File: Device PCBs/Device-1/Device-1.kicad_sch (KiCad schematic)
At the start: 29 parts, among them U2 MAX487E

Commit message: Device 1 PCB is finished
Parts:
- C1: renamed from C?; footprint (none) -> Capacitor_SMD:CP_Elec_6.3x5.7
- C2: renamed from C?; footprint (none) -> Capacitor_SMD:C_1206_3216Metric
- D1, D2, D3, D4, D5, D6, D7, D8, D9: renamed from D?; footprint (none) -> LED_SMD:LED_1206_3216Metric
- R1, R10, R11, R12, R13, R14, R15, R2, R3, R4, R5, R6, R7, R8, R9: renamed from R?; footprint (none) -> Resistor_SMD:R_1206_3216Metric
- U1: renamed from U?; footprint (none) -> Device_1_project_footprints:EBYTE-E32-433T20D
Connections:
- net EBYTE_AUX: now also A1.5 (D2); no longer A1.9 (D6)
- net EBYTE_RX: now also A1.7 (D4), D6.2 (A); no longer A1.8 (D5), D4.2 (A)
- net EBYTE_TX: now also A1.6 (D3), D4.2 (A); no longer A1.7 (D4), D6.2 (A)
- net M0: now also A1.9 (D6); no longer A1.5 (D2)
- net M1: now also A1.8 (D5); no longer A1.6 (D3)
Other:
- moved on the sheet: A1

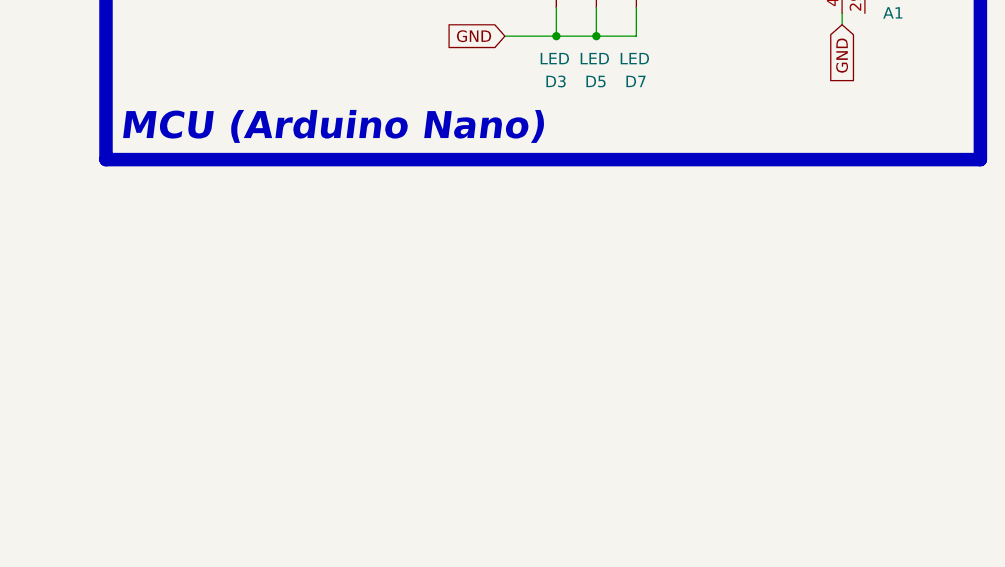
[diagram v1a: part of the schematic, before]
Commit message: slave config.h  and tescom_SDDPV2200M
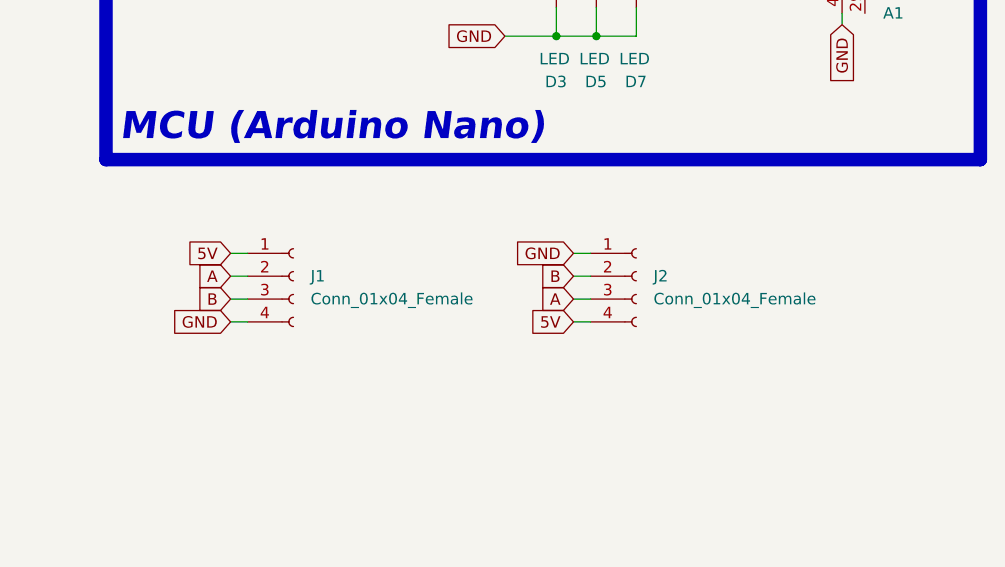
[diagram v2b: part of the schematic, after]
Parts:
- added J1: Conn_01x04_Female, Connector_PinSocket_2.54mm:PinSocket_1x04_P2.54mm_Vertical, symbol Connector:Conn_01x04_Female
- added J2: Conn_01x04_Female, Device_1_project_footprints:output_vias, symbol Connector:Conn_01x04_Female
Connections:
- net 5V: now also J1.1 (Pin_1), J2.4 (Pin_4)
- net A: now also J1.2 (Pin_2), J2.3 (Pin_3)
- net B: now also J1.3 (Pin_3), J2.2 (Pin_2)
- net GND: now also J1.4 (Pin_4), J2.1 (Pin_1)
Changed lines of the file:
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@@
+    (stroke (width 0) (type default) (color 0 0 0 0))
+  )
+  (wire (pts (xy 200.025 111.76) (xy 201.93 111.76))
     (stroke (width 0) (type default) (color 0 0 0 0))
   )
@@
     (stroke (width 0) (type default) (color 0 0 0 0))
   )
+  (wire (pts (xy 238.125 111.76) (xy 240.03 111.76))
+    (stroke (width 0) (type default) (color 0 0 0 0))
+  )
   (wire (pts (xy 59.182 91.821) (xy 76.327 91.821))
     (stroke (width 0) (type default) (color 0 0 0 0))
@@
     (stroke (width 0) (type default) (color 0 0 0 0))
   )
+  (wire (pts (xy 238.125 109.22) (xy 240.03 109.22))
+    (stroke (width 0) (type default) (color 0 0 0 0))
+  )
   (wire (pts (xy 248.92 54.61) (xy 255.27 54.61))
     (stroke (width 0) (type default) (color 0 0 0 0))
   )
+  (wire (pts (xy 238.125 114.3) (xy 240.03 114.3))
+    (stroke (width 0) (type default) (color 0 0 0 0))
+  )
   (wire (pts (xy 244.475 41.275) (xy 244.475 52.07))
     (stroke (width 0) (type default) (color 0 0 0 0))
@@
     (stroke (width 0) (type default) (color 0 0 0 0))
   )
+  (wire (pts (xy 238.125 116.84) (xy 240.03 116.84))
+    (stroke (width 0) (type default) (color 0 0 0 0))
+  )
   (wire (pts (xy 235.585 22.86) (xy 235.585 24.765))
     (stroke (width 0) (type default) (color 0 0 0 0))
@@
     (stroke (width 0) (type default) (color 0 0 0 0))
   )
+  (wire (pts (xy 200.025 109.22) (xy 201.93 109.22))
+    (stroke (width 0) (type default) (color 0 0 0 0))
+  )
   (wire (pts (xy 151.384 147.574) (xy 148.209 147.574))
     (stroke (width 0) (type default) (color 0 0 0 0))
@@
     (stroke (width 0.67) (type default) (color 0 0 0 0))
   )
+  (wire (pts (xy 200.025 114.3) (xy 201.93 114.3))
+    (stroke (width 0) (type default) (color 0 0 0 0))
+  )
   (wire (pts (xy 236.22 81.915) (xy 236.22 85.09))
+    (stroke (width 0) (type default) (color 0 0 0 0))
+  )
+  (wire (pts (xy 200.025 116.84) (xy 201.93 116.84))
     (stroke (width 0) (type default) (color 0 0 0 0))
   )
@@
     )
   )
+  (global_label "B" (shape input) (at 238.125 111.76 180) (fields_autoplaced)
+    (effects (font (size 1.27 1.27)) (justify right))
+    (property "Intersheet References" "${INTERSHEET_REFS}" (id 0) (at 234.4419 111.8394 0)
+      (effects (font (size 1.27 1.27)) (justify right) hide)
+    )
+  )
   (global_label "B" (shape input) (at 106.807 70.866 0) (fields_autoplaced)
     (effects (font (size 1.27 1.27)) (justify left))
@@
     )
   )
+  (global_label "GND" (shape input) (at 238.125 109.22 180) (fields_autoplaced)
+    (effects (font (size 1.27 1.27)) (justify right))
+    (property "Intersheet References" "${INTERSHEET_REFS}" (id 0) (at 231.8414 109.1406 0)
+      (effects (font (size 1.27 1.27)) (justify right) hide)
+    )
+  )
   (global_label "5V" (shape input) (at 151.384 165.354 0) (fields_autoplaced)
     (effects (font (size 1.27 1.27)) (justify left))
@@
     )
   )
+  (global_label "5V" (shape input) (at 200.025 109.22 180) (fields_autoplaced)
+    (effects (font (size 1.27 1.27)) (justify right))
+    (property "Intersheet References" "${INTERSHEET_REFS}" (id 0) (at 195.3138 109.2994 0)
+      (effects (font (size 1.27 1.27)) (justify right) hide)
+    )
+  )
   (global_label "RS485_SS_TX_PIN" (shape input) (at 50.927 78.486 180) (fields_autoplaced)
     (effects (font (size 1.27 1.27)) (justify right))
@@
     )
   )
+  (global_label "A" (shape input) (at 238.125 114.3 180) (fields_autoplaced)
+    (effects (font (size 1.27 1.27)) (justify right))
+    (property "Intersheet References" "${INTERSHEET_REFS}" (id 0) (at 234.6233 114.3794 0)
+      (effects (font (size 1.27 1.27)) (justify right) hide)
+    )
+  )
+  (global_label "GND" (shape input) (at 200.025 116.84 180) (fields_autoplaced)
+    (effects (font (size 1.27 1.27)) (justify right))
+    (property "Intersheet References" "${INTERSHEET_REFS}" (id 0) (at 193.7414 116.7606 0)
+      (effects (font (size 1.27 1.27)) (justify right) hide)
+    )
+  )
   (global_label "GND" (shape input) (at 228.6 22.86 180) (fields_autoplaced)
     (effects (font (size 1.27 1.27)) (justify right))
@@
     )
   )
+  (global_label "A" (shape input) (at 200.025 111.76 180) (fields_autoplaced)
+    (effects (font (size 1.27 1.27)) (justify right))
+    (property "Intersheet References" "${INTERSHEET_REFS}" (id 0) (at 196.5233 111.8394 0)
+      (effects (font (size 1.27 1.27)) (justify right) hide)
+    )
+  )
+  (global_label "B" (shape input) (at 200.025 114.3 180) (fields_autoplaced)
+    (effects (font (size 1.27 1.27)) (justify right))
+    (property "Intersheet References" "${INTERSHEET_REFS}" (id 0) (at 196.3419 114.3794 0)
+      (effects (font (size 1.27 1.27)) (justify right) hide)
+    )
+  )
   (global_label "EBYTE_RX" (shape input) (at 59.944 170.942 0) (fields_autoplaced)
     (effects (font (size 1.27 1.27)) (justify left))
@@
     (effects (font (size 1.27 1.27)) (justify right))
     (property "Intersheet References" "${INTERSHEET_REFS}" (id 0) (at 88.9476 93.3572 90)
+      (effects (font (size 1.27 1.27)) (justify right) hide)
+    )
+  )
+  (global_label "5V" (shape input) (at 238.125 116.84 180) (fields_autoplaced)
+    (effects (font (size 1.27 1.27)) (justify right))
+    (property "Intersheet References" "${INTERSHEET_REFS}" (id 0) (at 233.4138 116.9194 0)
       (effects (font (size 1.27 1.27)) (justify right) hide)
     )
@@
     (pin "2")
   )
+  (symbol (lib_id "Connector:Conn_01x04_Female") (at 207.01 111.76 0) (unit 1)
+    (in_bom yes) (on_board yes) (fields_autoplaced)
+    (property "Reference" "J1" (id 0) (at 208.915 111.7599 0)
+      (effects (font (size 1.27 1.27)) (justify left))
+    )
+    (property "Value" "Conn_01x04_Female" (id 1) (at 208.915 114.2999 0)
+      (effects (font (size 1.27 1.27)) (justify left))
+    )
+    (property "Footprint" "Connector_PinSocket_2.54mm:PinSocket_1x04_P2.54mm_Vertical" (id 2) (at 207.01 111.76 0)
+      (effects (font (size 1.27 1.27)) hide)
+    )
+    (property "Datasheet" "~" (id 3) (at 207.01 111.76 0)
+      (effects (font (size 1.27 1.27)) hide)
+    )
+    (pin "1")
+    (pin "2")
+    (pin "3")
+    (pin "4")
+  )
   (symbol (lib_id "Device:R") (at 244.475 28.575 180) (unit 1)
     (in_bom yes) (on_board yes)
@@
     (pin "1")
     (pin "2")
+  )
+  (symbol (lib_id "Connector:Conn_01x04_Female") (at 245.11 111.76 0) (unit 1)
+    (in_bom yes) (on_board yes) (fields_autoplaced)
+    (property "Reference" "J2" (id 0) (at 247.015 111.7599 0)
+      (effects (font (size 1.27 1.27)) (justify left))
+    )
+    (property "Value" "Conn_01x04_Female" (id 1) (at 247.015 114.2999 0)
+      (effects (font (size 1.27 1.27)) (justify left))
+    )
+    (property "Footprint" "Device_1_project_footprints:output_vias" (id 2) (at 245.11 111.76 0)
+      (effects (font (size 1.27 1.27)) hide)
+    )
+    (property "Datasheet" "~" (id 3) (at 245.11 111.76 0)
+      (effects (font (size 1.27 1.27)) hide)
+    )
+    (pin "1")
+    (pin "2")
+    (pin "3")
+    (pin "4")
   )
   (symbol (lib_id "Device:LED") (at 248.92 37.465 270) (unit 1)
@@
       (reference "D9") (unit 1) (value "LED") (footprint "LED_SMD:LED_1206_3216Metric")
     )
+    (path "/2e2cdef3-d221-46c3-96bb-35bd60ef0027"
+      (reference "J1") (unit 1) (value "Conn_01x04_Female") (footprint "Connector_PinSocket_2.54mm:PinSocket_1x04_P2.54mm_Vertical")
+    )
+    (path "/4897caee-f680-4d16-969b-7506d8f8b91f"
+      (reference "J2") (unit 1) (value "Conn_01x04_Female") (footprint "Device_1_project_footprints:output_vias")
+    )
     (path "/ababefe4-93dd-4ef0-80c7-1b4dc99fb798"

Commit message: Device 1 PCB is finished
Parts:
- added U10, U11, U12, U13, U14, U15, U16, U17, U18, U19, U20, U21, U22, U23, U3, U4, U5, U6, U7, U8, U9: signle_via, Device_1_project_footprints:single_via, symbol device_1_project_symbols:signle_via
- C1: footprint Capacitor_SMD:CP_Elec_6.3x5.7 -> Capacitor_SMD:CP_Elec_6.3x5.2
- D1, D2, D3, D8, D9: footprint LED_SMD:LED_1206_3216Metric -> Device_1_project_footprints:lm281B-3000K
- D4, D5, D6, D7: footprint LED_SMD:LED_1206_3216Metric -> Device_1_project_footprints:lm281B-6500K
- renumbered A1 to ArduinoNano
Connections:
- net 5V: now also J1.4 (Pin_4), U20.1 (Via); no longer J1.1 (Pin_1)
- net A: now also J2.2 (Pin_2); no longer J2.3 (Pin_3)
- net B: now also J1.1 (Pin_1), J2.1 (Pin_1); no longer J1.3 (Pin_3), J2.2 (Pin_2)
- net GND: now also J1.3 (Pin_3), J2.3 (Pin_3); no longer J1.4 (Pin_4), J2.1 (Pin_1)
- net at ArduinoNano.1 (D1/TX): now also U22.1 (Via)
- net at ArduinoNano.13 (D10): now also U3.1 (Via)
- net at ArduinoNano.14 (D11): now also U4.1 (Via)
- net at ArduinoNano.15 (D12): now also U5.1 (Via)
- net at ArduinoNano.16 (D13): now also U6.1 (Via)
- net at ArduinoNano.17 (3V3): now also U21.1 (Via)
- net at ArduinoNano.18 (AREF): now also U10.1 (Via)
- net at ArduinoNano.19 (A0): now also U11.1 (Via)
- net at ArduinoNano.2 (D0/RX): now also U23.1 (Via)
- net at ArduinoNano.20 (A1): now also U12.1 (Via)
- net at ArduinoNano.21 (A2): now also U13.1 (Via)
- net at ArduinoNano.22 (A3): now also U14.1 (Via)
- net at ArduinoNano.23 (A4): now also U15.1 (Via)
- net at ArduinoNano.24 (A5): now also U16.1 (Via)
- net at ArduinoNano.25 (A6): now also U17.1 (Via)
- net at ArduinoNano.26 (A7): now also U18.1 (Via)
- net at ArduinoNano.28 (~{RESET}): now also U8.1 (Via)
- net at ArduinoNano.29 (GND): now also U7.1 (Via)
- net at ArduinoNano.3 (~{RESET}): now also U9.1 (Via)
- net at ArduinoNano.30 (VIN): now also U19.1 (Via)
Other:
- moved on the sheet: ArduinoNano, D2, D3, D4, D5, D6, D7, D8, D9, R10, R11, R12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

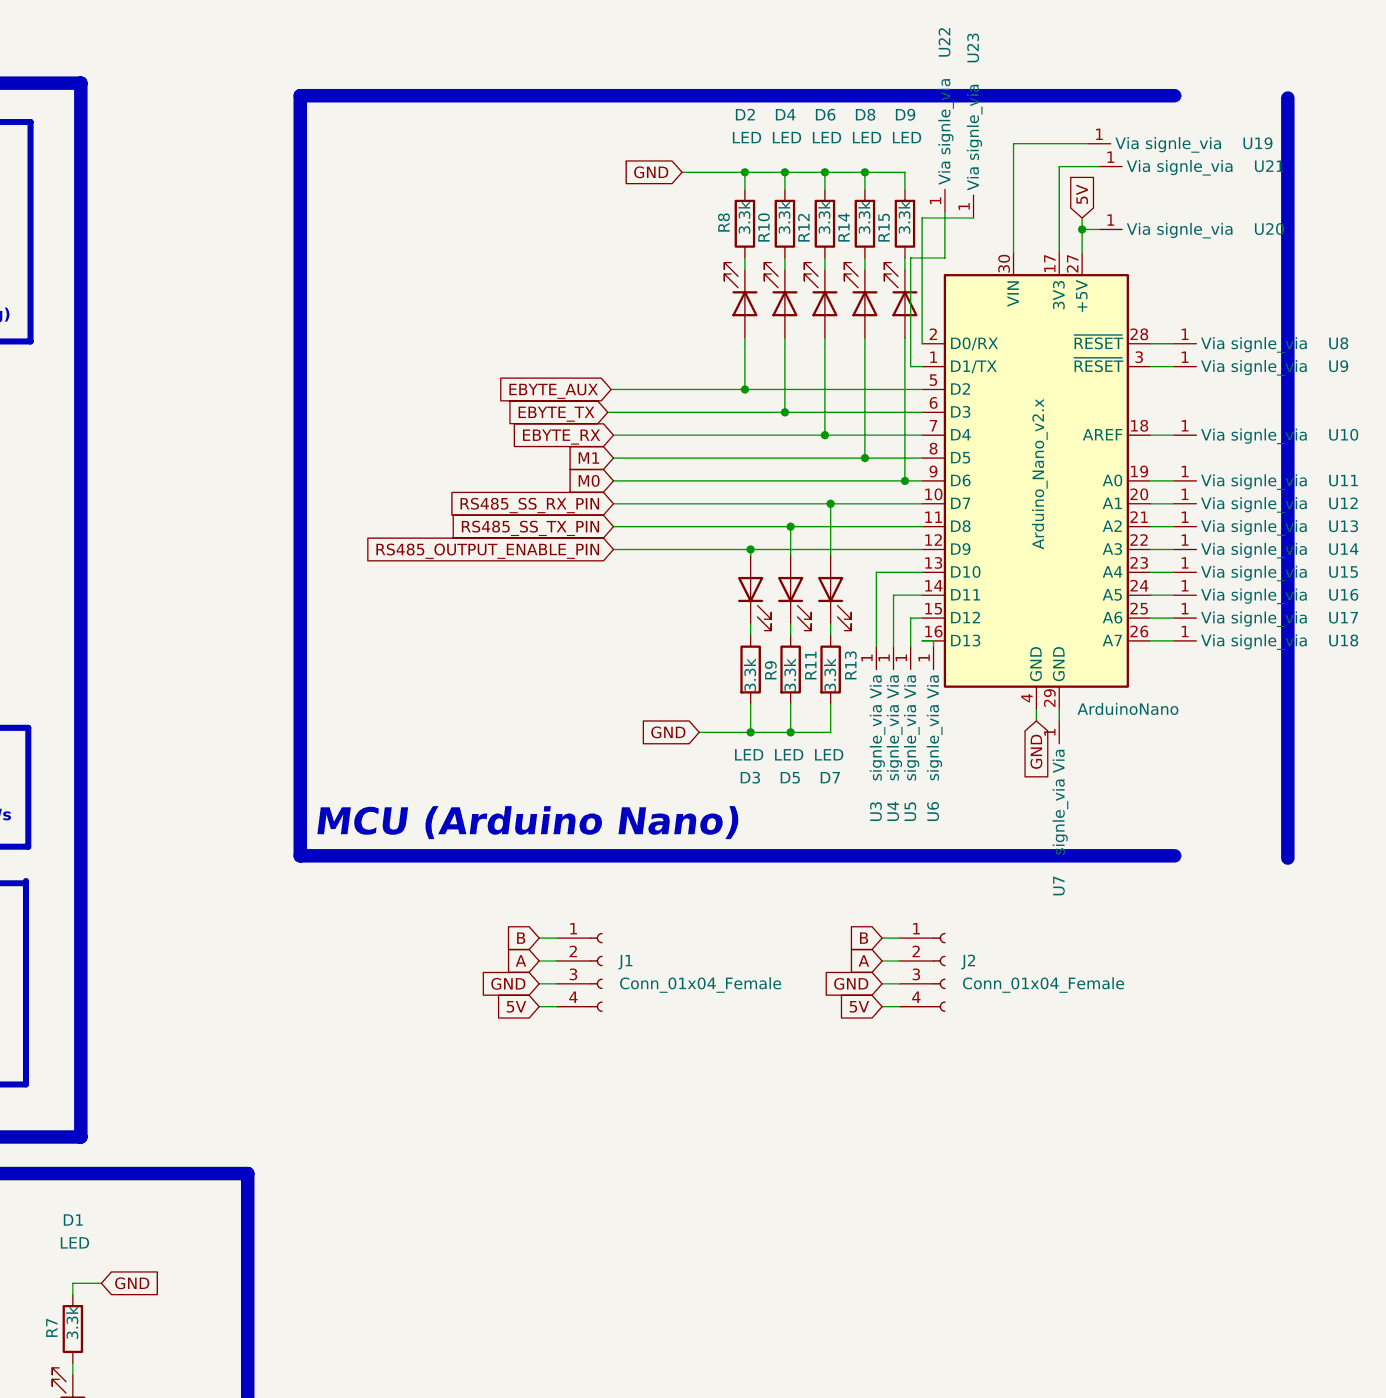
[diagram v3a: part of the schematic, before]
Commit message: PCB and slave fix
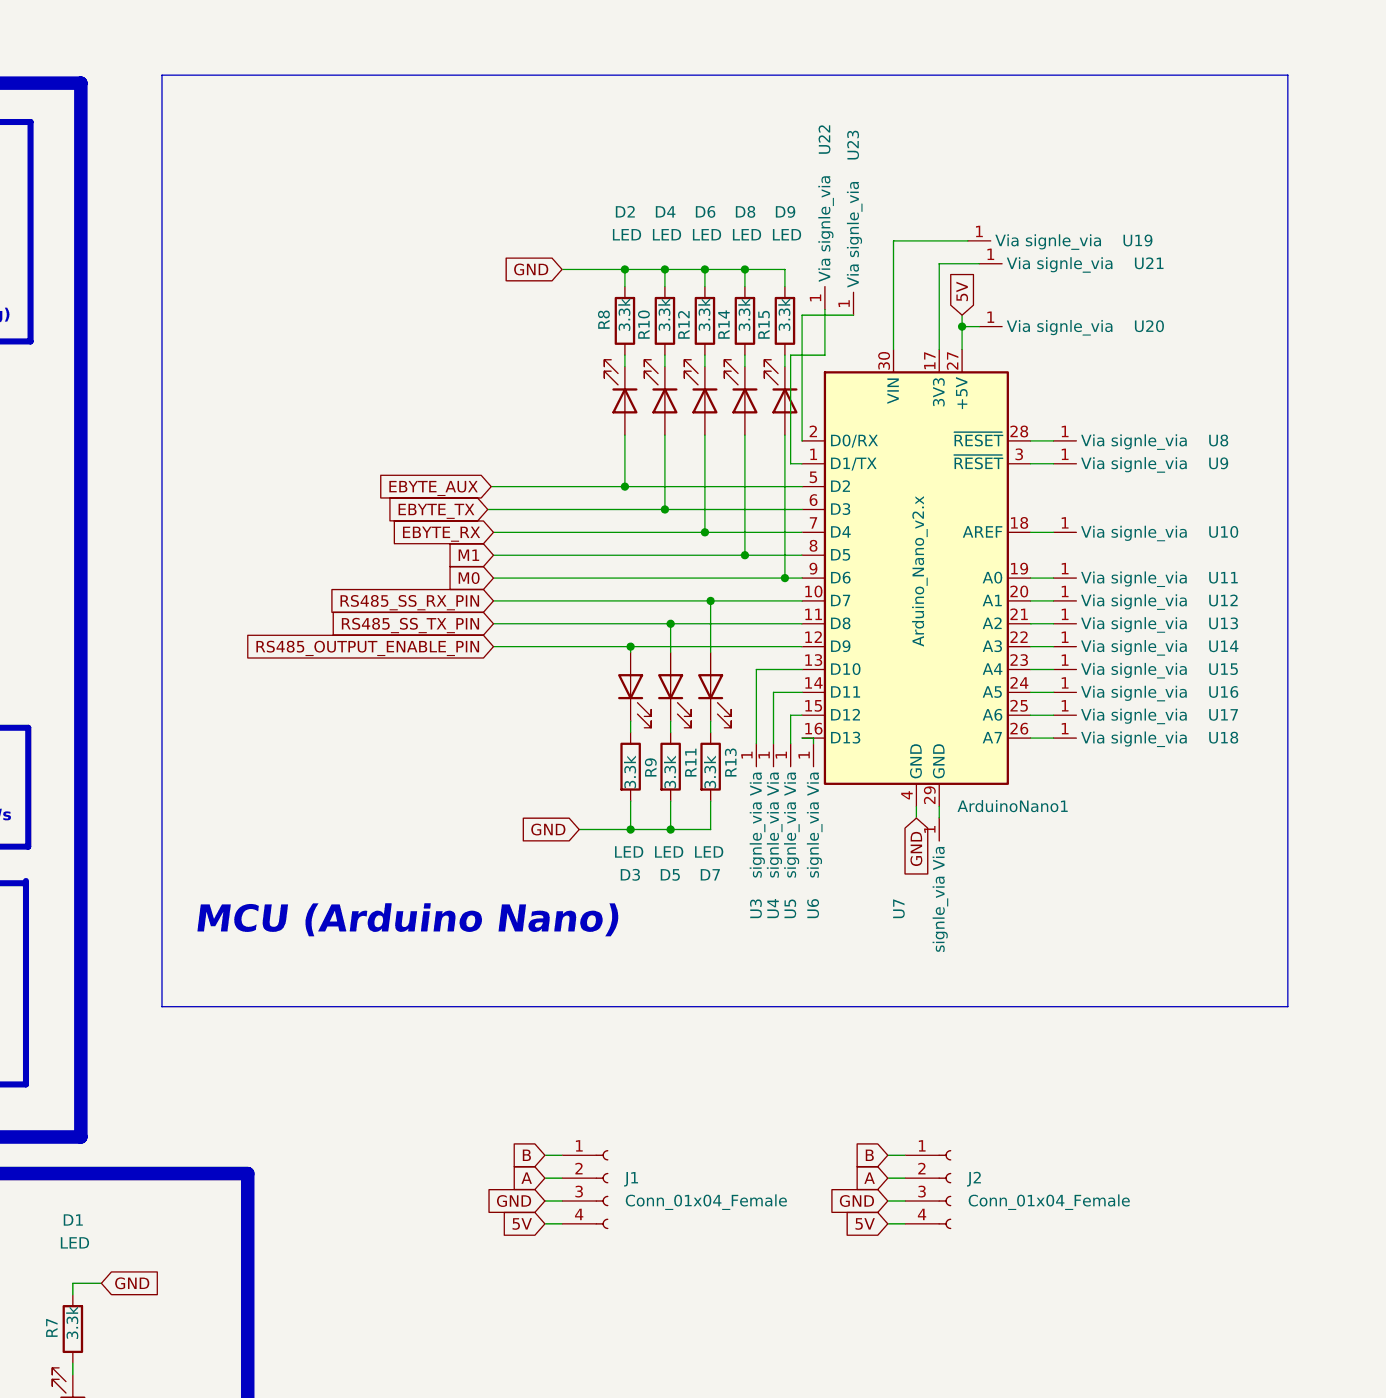
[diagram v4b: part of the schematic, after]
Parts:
- renumbered ArduinoNano to ArduinoNano1
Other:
- moved on the sheet: ArduinoNano1, D2, D3, D4, D5, D6, D7, D8, D9, J1, J2, R10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
